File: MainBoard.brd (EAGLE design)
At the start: 105.4 x 92.4 mm, 37 parts, among them IC2 2982-DRV8825, IC3 2982-DRV8825, IC4 2982-DRV8825, IC5 2982-DRV8825

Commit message: Pin 10 on the shift registers should be pulled high to enable the outputs
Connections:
- net GND: no longer SR1.10, SR2A.10, SR2B.10
- net VCC: now also SR1.10, SR2A.10, SR2B.10
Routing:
- net VCC: track 298.6 -> 336.2 mm, vias 4 -> 6
- net GND: track 62.1 -> 46.6 mm, vias 11 -> 10
- net Y_ENABLE: track 85.9 -> 88.8 mm
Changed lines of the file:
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@@
 <contactref element="SR2A" pad="13"/>
 <contactref element="SR2B" pad="13"/>
-<contactref element="SR2A" pad="10"/>
 <wire x1="6.57" y1="52.07" x2="6.57" y2="48.26" width="0.1524" layer="1"/>
-<contactref element="SR1" pad="10"/>
 <wire x1="6.57" y1="48.26" x2="7.62" y2="47.21" width="0.1524" layer="1"/>
 <wire x1="7.62" y1="47.21" x2="7.62" y2="38.1" width="0.1524" layer="1"/>
 <contactref element="SR1" pad="13"/>
 <contactref element="SR1" pad="8"/>
-<contactref element="SR2B" pad="10"/>
 <contactref element="C1" pad="2"/>
 <contactref element="C7" pad="2"/>
@@
 <wire x1="95.885" y1="33.655" x2="95.25" y2="33.02" width="0.254" layer="1"/>
 <via x="95.25" y="33.02" extent="1-16" drill="0.35"/>
-<wire x1="90.9066" y1="32.385" x2="91.5416" y2="33.02" width="0.1524" layer="1"/>
-<wire x1="91.5416" y1="33.02" x2="95.25" y2="33.02" width="0.1524" layer="1"/>
 <wire x1="90.9066" y1="28.575" x2="89.535" y2="28.575" width="0.1524" layer="1"/>
 <wire x1="89.535" y1="28.575" x2="88.9" y2="29.21" width="0.1524" layer="1"/>
@@
 <wire x1="71.71833125" y1="29.2354" x2="74.93" y2="32.44706875" width="0.1524" layer="1"/>
 <wire x1="74.93" y1="32.44706875" x2="74.93" y2="33.02" width="0.1524" layer="1"/>
-<wire x1="70.5866" y1="32.385" x2="69.9262" y2="33.0454" width="0.1524" layer="1"/>
-<wire x1="69.9262" y1="33.0454" x2="69.45486875" y2="33.0454" width="0.1524" layer="1"/>
-<wire x1="69.45486875" y1="33.0454" x2="67.31" y2="35.19026875" width="0.1524" layer="1"/>
-<wire x1="67.31" y1="35.19026875" x2="67.31" y2="39.37" width="0.1524" layer="1"/>
 <wire x1="27.88" y1="50.165" x2="26.035" y2="50.165" width="0.1524" layer="1"/>
 <wire x1="26.035" y1="50.165" x2="25.4" y2="49.53" width="0.1524" layer="1"/>
 <via x="25.4" y="49.53" extent="1-16" drill="0.35"/>
-<wire x1="62.9666" y1="50.165" x2="61.595" y2="50.165" width="0.1524" layer="1"/>
-<wire x1="61.595" y1="50.165" x2="60.96" y2="50.8" width="0.1524" layer="1"/>
-<via x="60.96" y="50.8" extent="1-16" drill="0.35"/>
 <wire x1="62.9666" y1="46.355" x2="62.3316" y2="45.72" width="0.1524" layer="1"/>
 <wire x1="62.3316" y1="45.72" x2="60.96" y2="45.72" width="0.1524" layer="1"/>
@@
 <contactref element="C7" pad="1"/>
 <contactref element="C6" pad="1"/>
-<wire x1="62.9666" y1="42.545" x2="63.82" y2="41.6916" width="0.254" layer="1"/>
+<wire x1="62.9666" y1="42.545" x2="63.5508" y2="41.9608" width="0.254" layer="1"/>
+<wire x1="63.5508" y1="41.9608" x2="63.82" y2="41.6916" width="0.254" layer="1"/>
 <wire x1="63.82" y1="41.6916" x2="63.82" y2="39.37" width="0.254" layer="1"/>
 <wire x1="70.5866" y1="24.765" x2="69.3166" y2="24.765" width="0.254" layer="1"/>
@@
 <wire x1="21.7202" y1="47.1798" x2="26.1648" y2="47.1798" width="0.254" layer="1"/>
 <wire x1="26.1648" y1="47.1798" x2="27.88" y2="48.895" width="0.254" layer="1"/>
+<contactref element="SR2A" pad="10"/>
+<contactref element="SR2B" pad="10"/>
+<contactref element="SR1" pad="10"/>
+<wire x1="64.77" y1="36.83" x2="69.215" y2="32.385" width="0.254" layer="1"/>
+<wire x1="69.215" y1="32.385" x2="70.5866" y2="32.385" width="0.254" layer="1"/>
+<wire x1="92.18563125" y1="32.0802" x2="92.5576" y2="31.70823125" width="0.254" layer="1"/>
+<wire x1="90.9066" y1="32.385" x2="91.2114" y2="32.0802" width="0.254" layer="1"/>
+<wire x1="91.2114" y1="32.0802" x2="92.18563125" y2="32.0802" width="0.254" layer="1"/>
+<wire x1="92.059375" y1="25.3746" x2="91.5162" y2="25.3746" width="0.254" layer="1"/>
+<wire x1="91.5162" y1="25.3746" x2="90.9066" y2="24.765" width="0.254" layer="1"/>
+<wire x1="92.5576" y1="31.70823125" x2="92.5576" y2="25.872825" width="0.254" layer="1"/>
+<wire x1="92.5576" y1="25.872825" x2="92.059375" y2="25.3746" width="0.254" layer="1"/>
+<wire x1="62.9666" y1="50.165" x2="56.515" y2="50.165" width="0.254" layer="1"/>
+<wire x1="56.515" y1="50.165" x2="55.88" y2="50.8" width="0.254" layer="1"/>
+<via x="55.88" y="50.8" extent="1-16" drill="0.35"/>
+<wire x1="55.88" y1="50.8" x2="59.69" y2="46.99" width="0.254" layer="16"/>
+<wire x1="59.69" y1="46.99" x2="59.69" y2="43.18" width="0.254" layer="16"/>
+<via x="59.69" y="43.18" extent="1-16" drill="0.35"/>
+<wire x1="59.69" y1="43.18" x2="61.788425" y2="43.18" width="0.254" layer="1"/>
+<wire x1="61.788425" y1="43.18" x2="61.813825" y2="43.1546" width="0.254" layer="1"/>
+<wire x1="61.813825" y1="43.1546" x2="62.357" y2="43.1546" width="0.254" layer="1"/>
+<wire x1="62.357" y1="43.1546" x2="62.9666" y2="42.545" width="0.254" layer="1"/>
 </signal>
 <signal name="+12V" class="1">
@@
 <wire x1="82.55" y1="27.94" x2="79.375" y2="24.765" width="0.1524" layer="1"/>
 <via x="80.01" y="31.75" extent="1-16" drill="0.35"/>
-<wire x1="80.01" y1="31.75" x2="69.1106" y2="42.6494" width="0.1524" layer="16"/>
+<wire x1="80.01" y1="31.75" x2="70.3806" y2="41.3794" width="0.1524" layer="16"/>
 <wire x1="41.91" y1="82.96829375" x2="41.91" y2="83.82" width="0.1524" layer="16"/>
-<wire x1="39.4462" y1="65.54550625" x2="39.4462" y2="80.50449375" width="0.1524" layer="16"/>
+<wire x1="39.4462" y1="60.46550625" x2="39.4462" y2="80.50449375" width="0.1524" layer="16"/>
 <wire x1="39.4462" y1="80.50449375" x2="41.91" y2="82.96829375" width="0.1524" layer="16"/>
-<wire x1="69.1106" y1="42.6494" x2="62.34230625" y2="42.6494" width="0.1524" layer="16"/>
-<wire x1="62.34230625" y1="42.6494" x2="39.4462" y2="65.54550625" width="0.1524" layer="16"/>
+<wire x1="70.3806" y1="41.3794" x2="58.53230625" y2="41.3794" width="0.1524" layer="16"/>
+<wire x1="58.53230625" y1="41.3794" x2="39.4462" y2="60.46550625" width="0.1524" layer="16"/>
 </signal>
 <signal name="N$26" class="1">

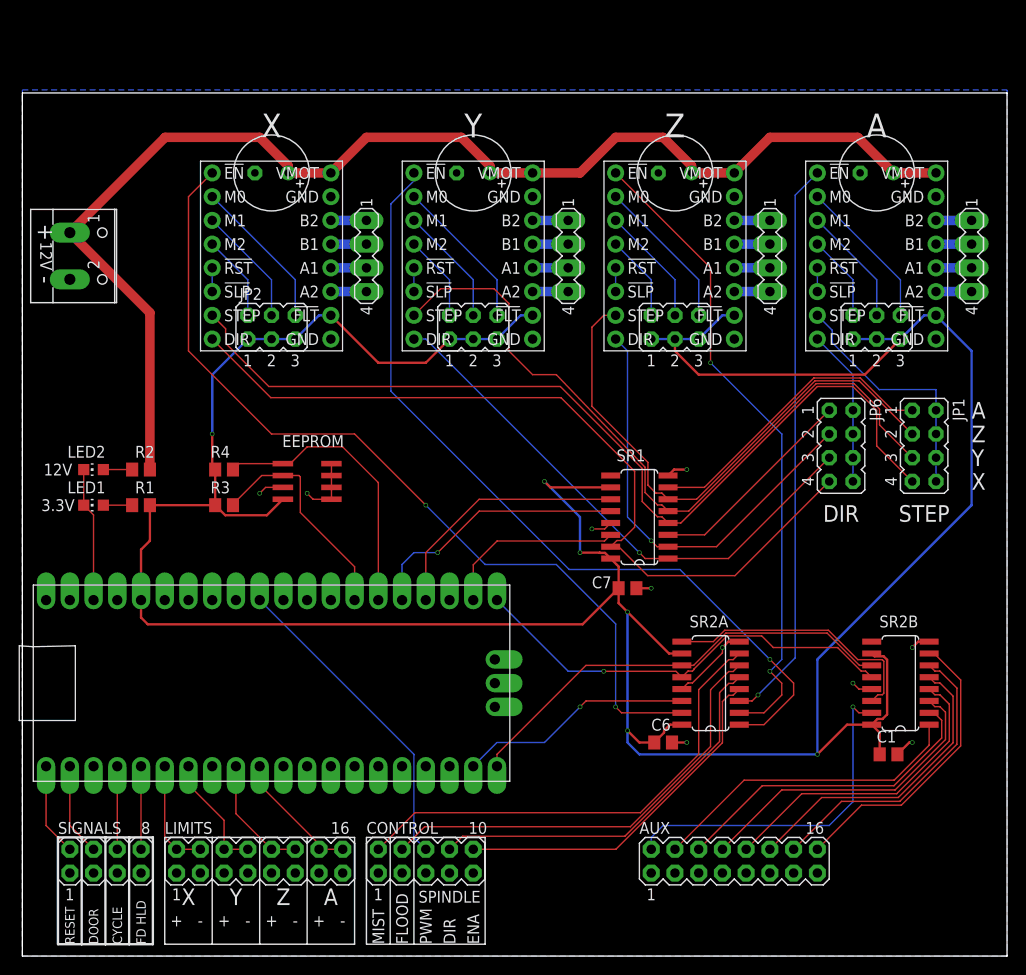
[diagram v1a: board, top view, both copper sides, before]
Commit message: Improved the layout a little bit and add some mounting holes
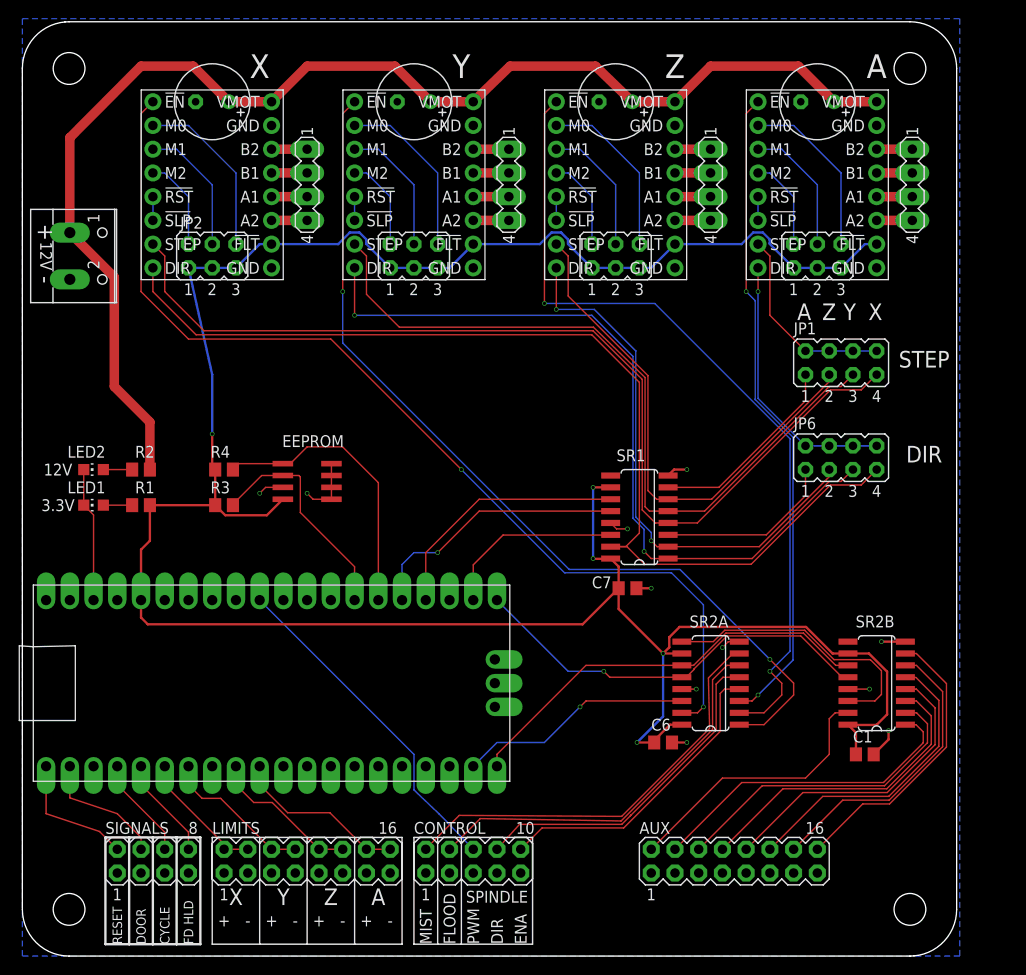
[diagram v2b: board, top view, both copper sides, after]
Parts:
- moved JP1 12.6 mm to (87.6, 63.5), turned to 0 degrees
- moved C2 9.92 mm to (20.3, 91.4)
- moved C3 9.92 mm to (41.9, 91.4)
- moved JP2 9.92 mm to (20.3, 74.9)
- moved JP3 9.92 mm to (41.9, 74.9)
- moved C4 9.92 mm to (63.5, 91.4)
- moved C5 9.92 mm to (85.1, 91.4)
- moved JP4 9.92 mm to (63.5, 74.9)
- moved JP5 9.92 mm to (85.1, 74.9)
- moved SV4 9.92 mm to (73.7, 82.5)
- moved IC2 9.92 mm to (20.3, 82.5)
- moved IC3 9.92 mm to (41.9, 82.5)
- moved SV3 9.92 mm to (52.1, 82.5)
- moved SV2 9.92 mm to (30.5, 82.5)
- moved IC4 9.92 mm to (63.5, 82.5)
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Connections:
- net N$13 renamed M0-X
- net N$14 renamed M1-X
- net N$15 renamed M2-X
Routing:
- net VCC: track 336.2 -> 274.4 mm, vias 6 -> 5
- net Y_DIR: track 58.7 -> 84.7 mm, vias 1 -> 2
- net X_DIR: track 89.3 -> 111.9 mm
- net Z_ENABLE: track 69.6 -> 88.6 mm
- net X_ENABLE: track 94.2 -> 108.4 mm
- net A'_DIR: track 16.8 -> 28.8 mm, vias 0 -> 1
- net Z_DIR: track 47.5 -> 59.0 mm, vias 1 -> 2
- net A_STEP: track 32.4 -> 21.3 mm
- net Y_ENABLE: track 88.8 -> 98.1 mm, vias 1 -> 2
- net A_ENABLE: track 60.8 -> 69.9 mm, vias 1 -> 2
- net AUX_OUT_1: track 36.9 -> 29.3 mm, vias 1 -> 0
- net X_STEP: track 99.6 -> 106.8 mm
- net MIST_ENA: track 51.4 -> 45.6 mm
- net A'_STEP: track 26.6 -> 21.2 mm
- net FLD_ENA: track 47.8 -> 42.4 mm
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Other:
- board size 105.4 x 92.4 mm -> 100 x 100 mm
